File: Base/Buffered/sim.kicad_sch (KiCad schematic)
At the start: 10 parts

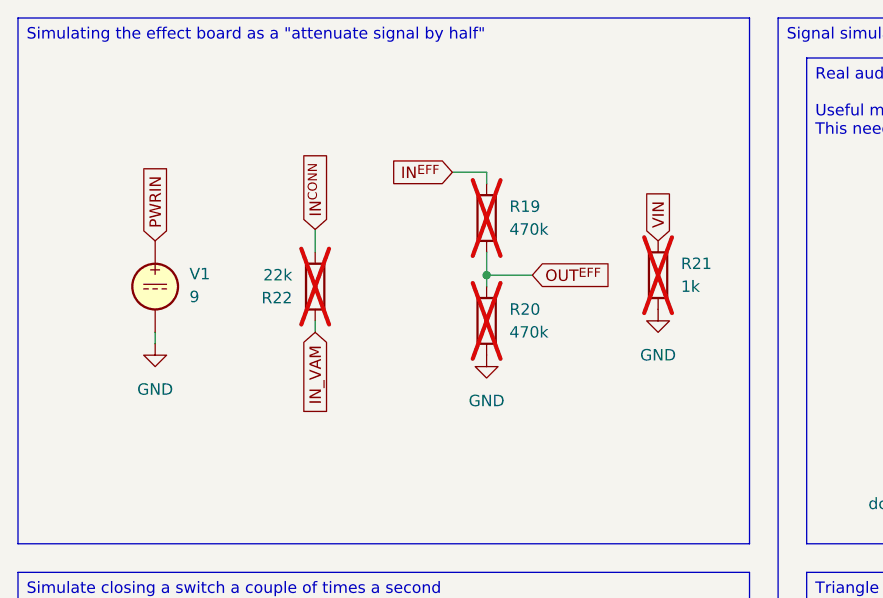
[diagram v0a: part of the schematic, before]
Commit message: Add negative power rail to the buffered base design
The negative voltage isn't actually _used_ anywhere yet, but this is
prep-work for making that buffered base board do the long promised
buffering, as I'm currently leaning towards opamps.

The LT3462A is very easy to use, but in a probably completely misguided
attempt at keeping any stray ground return currents on the power supply
side, I added a ground plane keepout.  No isolation, but an attempt to
at least make the easy path for any return currents to stay in that
"power supply area" and hopefully not show up around the analog parts.

Somebody who knows what they are about would probably tell me I'm just
making things worse.  But I'm a sw engineer, so pretty much by
definition I don't know anybody who knows what they are doing.

Signed-off-by: Linus Torvalds <torvalds@linux-foundation.org>
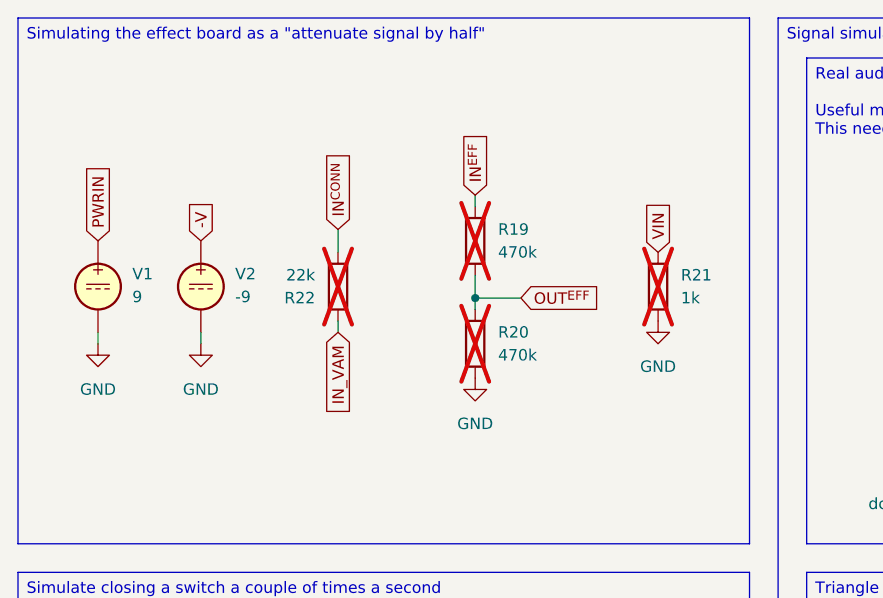
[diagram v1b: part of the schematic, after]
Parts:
- added V2: -9, symbol Simulation_SPICE:VDC
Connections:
- net GND: now also V2.2
- new net -V: V2.1
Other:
- moved on the sheet: R19, R20, R21, R22, V1

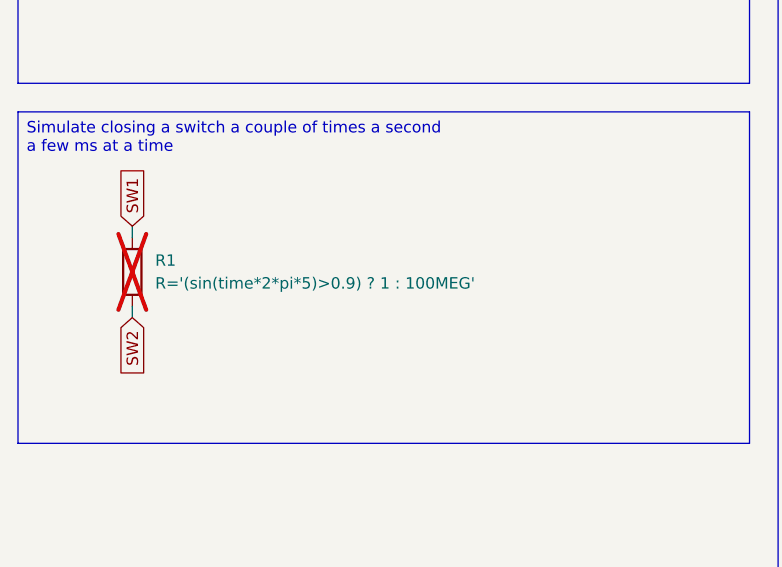
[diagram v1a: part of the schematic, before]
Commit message: Update the buffered base board
The JFET switching worked fine, but since this all started as an
exercise in using MOSFETs, let's just go all in on that, and use the
MOSFETs for switching the signal too.

Due to the body diode, you need two MOSFETs in series for the signal
switching, so it's four MOSFETs instead of two JFETs, but despite that
the end result is actually simpler.  And those dual MOSFET things are
common and dirt cheap, unlike the special matched JFET package.

Since I can just continue to use the dual complementary MOSFETs, I can
use PMOS for one signal and NMOS for the other, and share all the gate
circuit.  Plus no need for a diode to protect the gate current messing
with the signal.

Also update the resistor value in the switching circuit and make the
time constant be 100ms.  That seems to make it more reliable in testing,
although I'm not convinced my testing with the original value was all
that great.  The soft-switch circuit does seem to work, though.

Also, since the LED pin on the board connectors has never been used,
let's just re-purpose that as a negative voltage pin for the effect
board.  If some effect board wants to touch the LED status, it might as
well just connect to the LED itself.  Having access to a dual voltage
rail would seem to be a lot more important.

Finally - and probably most importantly for actual sound and current
effects boards - add a low-pass filter on the voltage lines.  Because as
expected, the negative power supply did add a lot of noise to the VIN
line.

The base board itself doesn't actually care, but the effects boards do.

An actual LDO would be better, but I don't have any simple fixed ones in
my parts library (except for the 5V one, which seems a bit sad).
Current effects boards don't use a lot of current and only care about
the voltage being stable, so let's try this simple model.

Signed-off-by: Linus Torvalds <torvalds@linux-foundation.org>
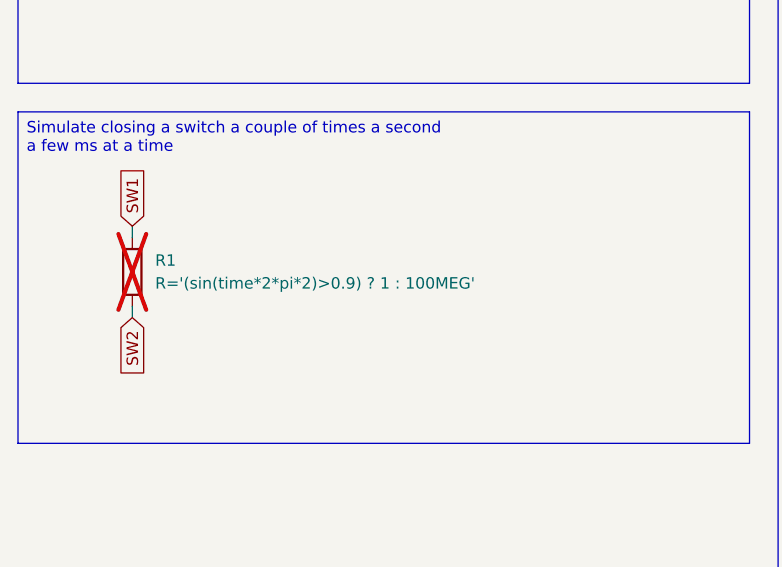
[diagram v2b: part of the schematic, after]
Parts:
- R1: value R='(sin(time*2*pi*5)>0.9) ? 1 : 100MEG' -> R='(sin(time*2*pi*2)>0.9) ? 1 : 100MEG'
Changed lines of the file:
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@@
 			)
 		)
-		(property "Value" "R='(sin(time*2*pi*5)>0.9)  ? 1 : 100MEG'"
+		(property "Value" "R='(sin(time*2*pi*2)>0.9)  ? 1 : 100MEG'"
 			(at 29.21 95.2499 0)
 			(effects

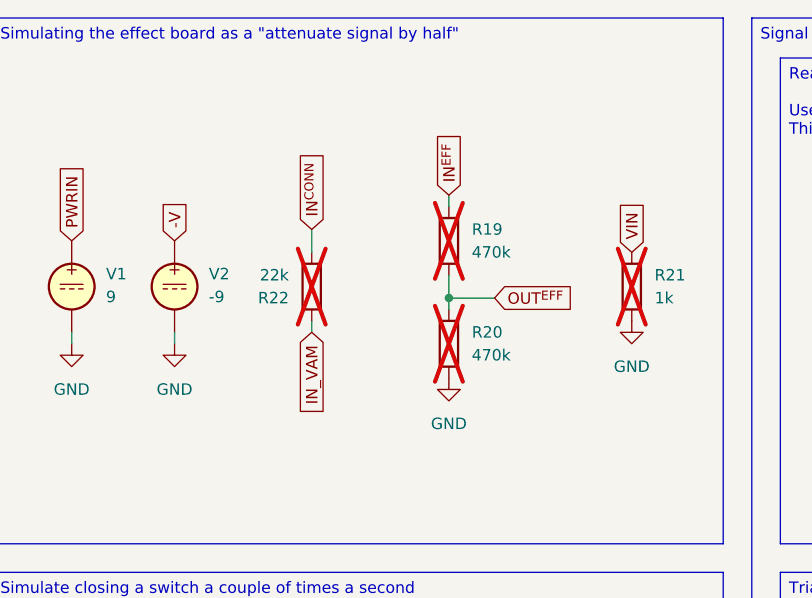
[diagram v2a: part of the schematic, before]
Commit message: Try LDO for positive voltage rail cleaning
As mentioned, I don't think I'll actually build this, because it seems
pointlessly complicated.  But I did the basic design and layout for it
just in case.

I think I'll go back to the single-rail design and keep the MOSFET
switching.

I also think I need to come up with a new project.  I'm kind of running
out of ideas of small projects to do that I can build and test.  I like
the switching circuit, but I'm losing interest in the effects board side
since I still can't actually play guitar.

Signed-off-by: Linus Torvalds <torvalds@linux-foundation.org>
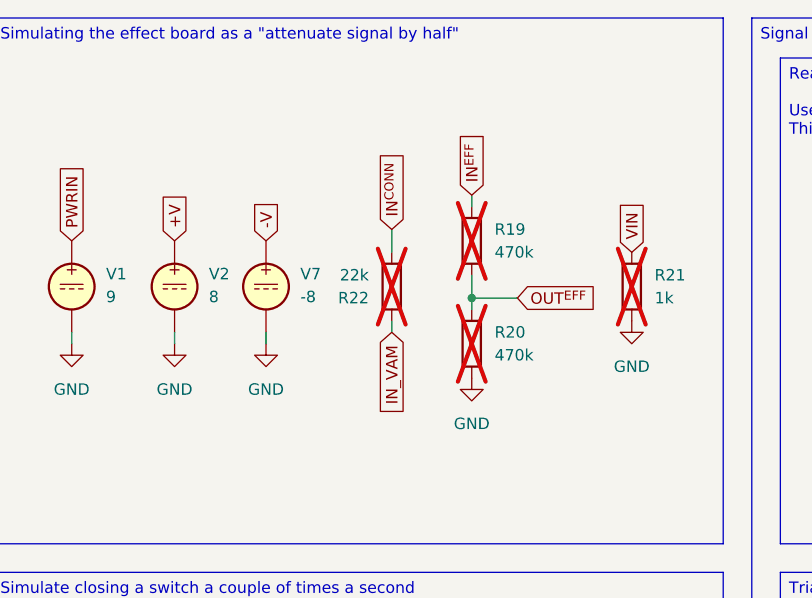
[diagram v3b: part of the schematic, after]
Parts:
- added V7: -8, symbol Simulation_SPICE:VDC
- V2: value -9 -> 8
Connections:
- net -V: now also V7.1; no longer V2.1
- net GND: now also V7.2
- new net +V: V2.1
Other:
- moved on the sheet: R19, R20, R22
